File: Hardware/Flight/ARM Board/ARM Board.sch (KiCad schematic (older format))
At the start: 1 part, among them U1 STM32L4x6RxT6

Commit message: Added footprint and sch for SD logger, pull up resistor on data out as per documentation found in Datasheets and Documentation folder
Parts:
- added J?: SD_WM6698CT-ND, symbol ARMlib:SD_WM6698CT-ND
- added R?: R, Resistors_SMD:R_0603, symbol Device:R
- U1: symbol STM32L4x6RxT6 -> symbols:STM32L4x6RxT6
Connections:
- net labels added: VDD
- wire segments 0 -> 3
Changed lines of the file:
@@
-EESchema Schematic File Version 2
-LIBS:power
-LIBS:device
-LIBS:switches
-LIBS:relays
-LIBS:motors
-LIBS:transistors
-LIBS:conn
-LIBS:linear
-LIBS:regul
-LIBS:74xx
-LIBS:cmos4000
-LIBS:adc-dac
-LIBS:memory
-LIBS:xilinx
-LIBS:microcontrollers
-LIBS:dsp
-LIBS:microchip
-LIBS:analog_switches
-LIBS:motorola
-LIBS:texas
-LIBS:intel
-LIBS:audio
-LIBS:interface
-LIBS:digital-audio
-LIBS:philips
-LIBS:display
-LIBS:cypress
-LIBS:siliconi
-LIBS:opto
-LIBS:atmel
-LIBS:contrib
-LIBS:valves
-LIBS:symbols
-EELAYER 25 0
+EESchema Schematic File Version 4
+LIBS:ARM Board-cache
+EELAYER 26 0
 EELAYER END
 $Descr A4 11693 8268
@@
 $EndDescr
 $Comp
-L STM32L4x6RxT6 U1
+L symbols:STM32L4x6RxT6 U1
 U 1 1 5BE24A8B
 P 2300 1950
@@
 $EndComp
 $Comp
-L STM32L4x6RxT6 U1
+L symbols:STM32L4x6RxT6 U1
 U 2 1 5BE24AAA
 P 7050 2200
@@
 	1    0    0    -1
 $EndComp
+$Comp
+L ARMlib:SD_WM6698CT-ND J?
+U 1 1 5BE5108C
+P 8550 5100
+F 0 "J?" H 9028 5202 60  0000 L CNN
+F 1 "SD_WM6698CT-ND" H 9028 5096 60  0000 L CNN
+F 2 "" V 8500 5000 60  0001 C CNN
+F 3 "" V 8500 5000 60  0001 C CNN
+	1    8550 5100
+	1    0    0    -1
+$EndComp
+$Comp
+L Device:R R?
+U 1 1 5BE5134B
+P 7850 4200
+F 0 "R?" H 7920 4246 50  0000 L CNN
+F 1 "R" H 7920 4155 50  0000 L CNN
+F 2 "Resistors_SMD:R_0603" V 7780 4200 50  0001 C CNN
+F 3 "~" H 7850 4200 50  0001 C CNN
+	1    7850 4200
+	1    0    0    -1
+$EndComp
+Wire Wire Line
+	7850 4350 7850 4450
+Wire Wire Line
+	7850 4450 8050 4450
+$Comp
+L power:VDD #PWR?
+U 1 1 5BE51D76
+P 7850 3700
+F 0 "#PWR?" H 7850 3550 50  0001 C CNN
+F 1 "VDD" H 7867 3873 50  0000 C CNN
+F 2 "" H 7850 3700 50  0001 C CNN
+F 3 "" H 7850 3700 50  0001 C CNN
+	1    7850 3700
+	1    0    0    -1
+$EndComp
+Wire Wire Line
+	7850 3700 7850 4050
 $EndSCHEMATC

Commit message: Added footprint and sch for IO connector and USB
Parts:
- added J? (x2): Conn_01x20_Female, ARMlib:IO_Connector, symbol ARMlib:Conn_01x20_Female
- added J?: USB_B_Micro, ARMlib:USB_Micro-B_Amphenol_10118193-0001LF, symbol Connector:USB_B_Micro
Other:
- moved on the sheet: R?, U1A, U1B
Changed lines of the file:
@@
 L symbols:STM32L4x6RxT6 U1
 U 1 1 5BE24A8B
-P 2300 1950
-F 0 "U1" H 3250 2500 60  0000 C CNN
-F 1 "STM32L4x6RxT6" H 3250 2400 60  0000 C CNN
-F 2 "STM32L4x6RxT6:STM32L4x6RxT6" H 3150 2300 60  0001 C CNN
-F 3 "" H 2300 2050 60  0000 C CNN
-	1    2300 1950
+P 5450 2700
+F 0 "U1" H 6400 3250 60  0000 C CNN
+F 1 "STM32L4x6RxT6" H 6400 3150 60  0000 C CNN
+F 2 "STM32L4x6RxT6:STM32L4x6RxT6" H 6300 3050 60  0001 C CNN
+F 3 "" H 5450 2800 60  0000 C CNN
+	1    5450 2700
 	1    0    0    -1
 $EndComp
@@
 L symbols:STM32L4x6RxT6 U1
 U 2 1 5BE24AAA
-P 7050 2200
-F 0 "U1" H 8000 2750 60  0000 C CNN
-F 1 "STM32L4x6RxT6" H 8000 2650 60  0000 C CNN
-F 2 "LQFP64-10x10mm" H 7900 2550 60  0001 C CNN
-F 3 "" H 7050 2300 60  0000 C CNN
-	2    7050 2200
+P 2400 1450
+F 0 "U1" H 3350 2000 60  0000 C CNN
+F 1 "STM32L4x6RxT6" H 3350 1900 60  0000 C CNN
+F 2 "LQFP64-10x10mm" H 3250 1800 60  0001 C CNN
+F 3 "" H 2400 1550 60  0000 C CNN
+	2    2400 1450
 	1    0    0    -1
 $EndComp
@@
 L ARMlib:SD_WM6698CT-ND J?
 U 1 1 5BE5108C
-P 8550 5100
-F 0 "J?" H 9028 5202 60  0000 L CNN
-F 1 "SD_WM6698CT-ND" H 9028 5096 60  0000 L CNN
-F 2 "" V 8500 5000 60  0001 C CNN
-F 3 "" V 8500 5000 60  0001 C CNN
-	1    8550 5100
+P 10300 5050
+F 0 "J?" H 10778 5152 60  0000 L CNN
+F 1 "SD_WM6698CT-ND" H 10778 5046 60  0000 L CNN
+F 2 "" V 10250 4950 60  0001 C CNN
+F 3 "" V 10250 4950 60  0001 C CNN
+	1    10300 5050
 	1    0    0    -1
 $EndComp
@@
 L Device:R R?
 U 1 1 5BE5134B
-P 7850 4200
-F 0 "R?" H 7920 4246 50  0000 L CNN
-F 1 "R" H 7920 4155 50  0000 L CNN
-F 2 "Resistors_SMD:R_0603" V 7780 4200 50  0001 C CNN
-F 3 "~" H 7850 4200 50  0001 C CNN
-	1    7850 4200
+P 9600 4150
+F 0 "R?" H 9670 4196 50  0000 L CNN
+F 1 "R" H 9670 4105 50  0000 L CNN
+F 2 "Resistors_SMD:R_0603" V 9530 4150 50  0001 C CNN
+F 3 "~" H 9600 4150 50  0001 C CNN
+	1    9600 4150
 	1    0    0    -1
 $EndComp
 Wire Wire Line
-	7850 4350 7850 4450
+	9600 4300 9600 4400
 Wire Wire Line
-	7850 4450 8050 4450
+	9600 4400 9800 4400
 $Comp
 L power:VDD #PWR?
 U 1 1 5BE51D76
-P 7850 3700
-F 0 "#PWR?" H 7850 3550 50  0001 C CNN
-F 1 "VDD" H 7867 3873 50  0000 C CNN
-F 2 "" H 7850 3700 50  0001 C CNN
-F 3 "" H 7850 3700 50  0001 C CNN
-	1    7850 3700
+P 9600 3650
+F 0 "#PWR?" H 9600 3500 50  0001 C CNN
+F 1 "VDD" H 9617 3823 50  0000 C CNN
+F 2 "" H 9600 3650 50  0001 C CNN
+F 3 "" H 9600 3650 50  0001 C CNN
+	1    9600 3650
 	1    0    0    -1
 $EndComp
 Wire Wire Line
-	7850 3700 7850 4050
+	9600 3650 9600 4000
+$Comp
+L ARMlib:Conn_01x20_Female J?
+U 1 1 5BE939D5
+P 950 6450
+F 0 "J?" H 944 5175 50  0000 C CNN
+F 1 "Conn_01x20_Female" H 944 5266 50  0000 C CNN
+F 2 "ARMlib:IO_Connector" H 1000 6400 50  0001 C CNN
+F 3 "~" H 1000 6400 50  0001 C CNN
+	1    950  6450
+	-1   0    0    1
+$EndComp
+$Comp
+L ARMlib:Conn_01x20_Female J?
+U 1 1 5BE93A8D
+P 1000 4050
+F 0 "J?" H 994 2775 50  0000 C CNN
+F 1 "Conn_01x20_Female" H 994 2866 50  0000 C CNN
+F 2 "ARMlib:IO_Connector" H 1050 4000 50  0001 C CNN
+F 3 "~" H 1050 4000 50  0001 C CNN
+	1    1000 4050
+	-1   0    0    1
+$EndComp
+$Comp
+L Connector:USB_B_Micro J?
+U 1 1 5BE9421F
+P 1100 1650
+F 0 "J?" H 1155 2117 50  0000 C CNN
+F 1 "USB_B_Micro" H 1155 2026 50  0000 C CNN
+F 2 "ARMlib:USB_Micro-B_Amphenol_10118193-0001LF" H 1250 1600 50  0001 C CNN
+F 3 "~" H 1250 1600 50  0001 C CNN
+	1    1100 1650
+	1    0    0    -1
+$EndComp
 $EndSCHEMATC

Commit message: Added crystal, caps and MsP430
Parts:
- added C1, C2: C_Small, symbol Device:C_Small
- added U2: MSP430FR2355, ARMlib:48-LQFP, symbol MSP430FR2355:MSP430FR2355
- added Y1: Crystal_GND23, ARMlib:MC-306 32.7680K, symbol Device:Crystal_GND23
- gave numbers to parts that had none: 5
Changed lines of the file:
@@
 $EndComp
 $Comp
-L ARMlib:SD_WM6698CT-ND J?
+L ARMlib:SD_WM6698CT-ND J3
 U 1 1 5BE5108C
 P 10300 5050
-F 0 "J?" H 10778 5152 60  0000 L CNN
+F 0 "J3" H 10778 5152 60  0000 L CNN
 F 1 "SD_WM6698CT-ND" H 10778 5046 60  0000 L CNN
 F 2 "" V 10250 4950 60  0001 C CNN
@@
 $EndComp
 $Comp
-L Device:R R?
+L Device:R R1
 U 1 1 5BE5134B
 P 9600 4150
-F 0 "R?" H 9670 4196 50  0000 L CNN
+F 0 "R1" H 9670 4196 50  0000 L CNN
 F 1 "R" H 9670 4105 50  0000 L CNN
 F 2 "Resistors_SMD:R_0603" V 9530 4150 50  0001 C CNN
@@
 	9600 4400 9800 4400
 $Comp
-L power:VDD #PWR?
+L power:VDD #PWR0101
 U 1 1 5BE51D76
 P 9600 3650
-F 0 "#PWR?" H 9600 3500 50  0001 C CNN
+F 0 "#PWR0101" H 9600 3500 50  0001 C CNN
 F 1 "VDD" H 9617 3823 50  0000 C CNN
 F 2 "" H 9600 3650 50  0001 C CNN
@@
 	9600 3650 9600 4000
 $Comp
-L ARMlib:Conn_01x20_Female J?
+L ARMlib:Conn_01x20_Female J4
 U 1 1 5BE939D5
 P 950 6450
-F 0 "J?" H 944 5175 50  0000 C CNN
+F 0 "J4" H 944 5175 50  0000 C CNN
 F 1 "Conn_01x20_Female" H 944 5266 50  0000 C CNN
 F 2 "ARMlib:IO_Connector" H 1000 6400 50  0001 C CNN
@@
 $EndComp
 $Comp
-L ARMlib:Conn_01x20_Female J?
+L ARMlib:Conn_01x20_Female J2
 U 1 1 5BE93A8D
 P 1000 4050
-F 0 "J?" H 994 2775 50  0000 C CNN
+F 0 "J2" H 994 2775 50  0000 C CNN
 F 1 "Conn_01x20_Female" H 994 2866 50  0000 C CNN
 F 2 "ARMlib:IO_Connector" H 1050 4000 50  0001 C CNN
@@
 $EndComp
 $Comp
-L Connector:USB_B_Micro J?
+L Connector:USB_B_Micro J1
 U 1 1 5BE9421F
 P 1100 1650
-F 0 "J?" H 1155 2117 50  0000 C CNN
+F 0 "J1" H 1155 2117 50  0000 C CNN
 F 1 "USB_B_Micro" H 1155 2026 50  0000 C CNN
 F 2 "ARMlib:USB_Micro-B_Amphenol_10118193-0001LF" H 1250 1600 50  0001 C CNN
@@
 	1    0    0    -1
 $EndComp
+$Comp
+L Device:Crystal_GND23 Y1
+U 1 1 5BF7653E
+P 9250 5900
+F 0 "Y1" H 9250 6250 50  0000 L CNN
+F 1 "Crystal_GND23" H 9000 6150 50  0000 L CNN
+F 2 "ARMlib:MC-306 32.7680K" H 9250 5900 50  0001 C CNN
+F 3 "~" H 9250 5900 50  0001 C CNN
+	1    9250 5900
+	1    0    0    -1
+$EndComp
+$Comp
+L Device:C_Small C2
+U 1 1 5BF76C5B
+P 9550 6150
+F 0 "C2" H 9642 6196 50  0000 L CNN
+F 1 "C_Small" H 9642 6105 50  0000 L CNN
+F 2 "" H 9550 6150 50  0001 C CNN
+F 3 "~" H 9550 6150 50  0001 C CNN
+	1    9550 6150
+	1    0    0    -1
+$EndComp
+$Comp
+L Device:C_Small C1
+U 1 1 5BF76CF0
+P 8900 6150
+F 0 "C1" H 8992 6196 50  0000 L CNN
+F 1 "C_Small" H 8992 6105 50  0000 L CNN
+F 2 "" H 8900 6150 50  0001 C CNN
+F 3 "~" H 8900 6150 50  0001 C CNN
+	1    8900 6150
+	1    0    0    -1
+$EndComp
+$Comp
+L MSP430FR2355:MSP430FR2355 U2
+U 1 1 5BF776E6
+P 14350 2100
+F 0 "U2" H 14400 3587 60  0000 C CNN
+F 1 "MSP430FR2355" H 14400 3481 60  0000 C CNN
+F 2 "ARMlib:48-LQFP" H 14350 650 60  0001 C CNN
+F 3 "http://www.ti.com/lit/ds/symlink/msp430fr2355.pdf" H 14350 550 60  0001 C CNN
+F 4 "296-50261-1-ND" H 14350 450 60  0001 C CNN "Digi-Key Part Number"
+	1    14350 2100
+	1    0    0    -1
+$EndComp

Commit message: power supply for stm32
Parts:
- added C? (x3): 100nF, symbol Device:C
- added C?: 1uF, symbol Device:C
- added C?: 10uF, symbol Device:C
- added C?: 100uF, symbol Device:C
- added L?: Ferrite_Bead, symbol Device:Ferrite_Bead
- J2, J4: symbol ARMlib:Conn_01x20_Female -> ARM-Board-rescue:Conn_01x20_Female-ARMlib
- J3: symbol ARMlib:SD_WM6698CT-ND -> ARM-Board-rescue:SD_WM6698CT-ND-ARMlib
- U1: symbol symbols:STM32L4x6RxT6 -> ARM-Board-rescue:STM32L4x6RxT6-symbols
- U2: symbol MSP430FR2355:MSP430FR2355 -> ARM-Board-rescue:MSP430FR2355-MSP430FR2355
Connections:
- net labels added: GND
- wire segments 3 -> 35
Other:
- note added: "TODO\n-ADD RAM\n-ADD CANBUS\n-ADD USB TO UART\n-POWER SWITCH"

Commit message: Added USB to UART and connected XTAL
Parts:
- added C? (x2): 47pF, symbol Device:C
- added C? (x2): 100nF, symbol Device:C
- added C?: 4.7uF, symbol Device:C
- added FB?: Ferrite_Bead, symbol Device:Ferrite_Bead
- added J?: SD_WM6698CT-ND, symbol ARM-Board-rescue:SD_WM6698CT-ND-ARMlib
- added J?: USB_OTG, symbol Connector:USB_OTG
- added R?: R, Resistors_SMD:R_0603, symbol Device:R
- added R? (x2): 27, symbol Device:R
- added R? (x4): 10K, symbol Device:R
- added U?: FT230XS, Package_SO:SSOP-16_3.9x4.9mm_P0.635mm, symbol Interface_USB:FT230XS
- U1: Package (none) -> 64LQFP
- U1: footprint LQFP64-10x10mm -> STM32L4x6RxT6:STM32L4x6RxT6
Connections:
- net labels added: RXD, TXD, VBUS, VCCIO, ~CTS, ~RTS
- wire segments 35 -> 114
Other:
- moved on the sheet: C1, C2, J3, R1, U1A, U2, Y1

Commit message: Completion of previous commit
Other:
- note added: "Ground other XTAL pins? Floating in datasheet...\n"
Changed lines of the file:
@@
 Wire Wire Line
 	6000 7250 6000 7400
+Text Notes 4000 7400 0    50   ~ 0
+Ground other XTAL pins? Floating in datasheet...\n
 $EndSCHEMATC

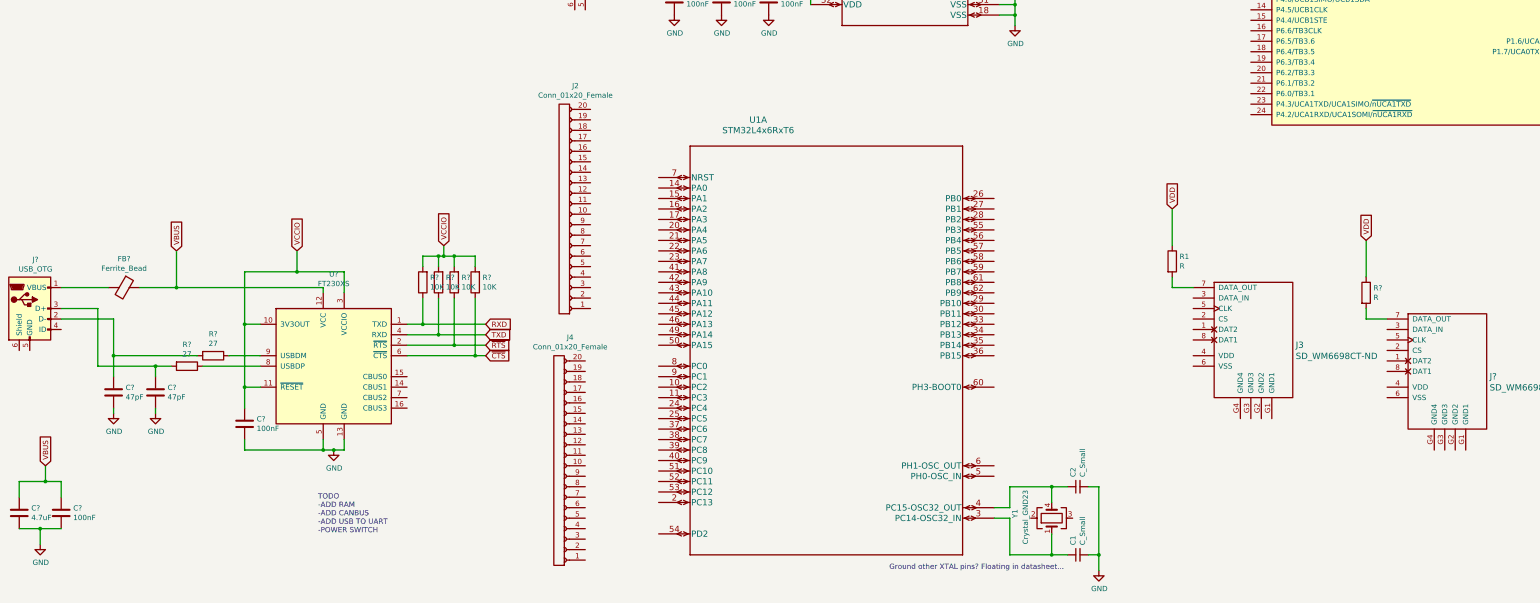
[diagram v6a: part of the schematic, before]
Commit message: RAM and cleanup
Added RAM module, seperate sch for USB to UART, SPI pin net flags
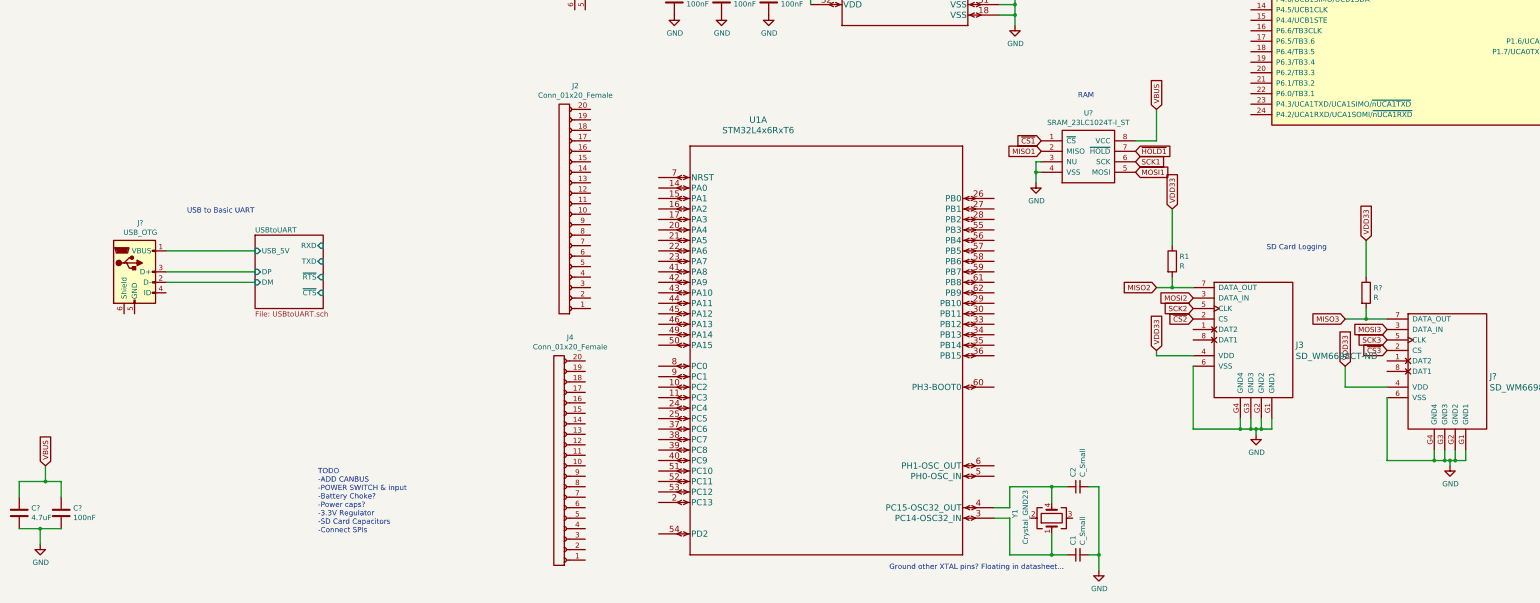
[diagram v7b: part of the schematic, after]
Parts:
- removed C? (x2): 47pF, symbol Device:C
- removed C?: 100nF, symbol Device:C
- removed FB?: Ferrite_Bead, symbol Device:Ferrite_Bead
- removed R? (x2): 27, symbol Device:R
- removed R? (x4): 10K, symbol Device:R
- removed U?: FT230XS, Package_SO:SSOP-16_3.9x4.9mm_P0.635mm, symbol Interface_USB:FT230XS
- added U?: SRAM_23LC1024T-I_ST, Housings_SSOP:TSSOP-8_4.4x3mm_Pitch0.65mm, symbol ARMlib:SRAM_23LC1024T-I_ST
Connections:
- net GND: now also J3.6 (VSS), J3.G1 (GND1), J3.G2 (GND2), J3.G3 (GND3), J3.G4 (GND4), J?.6 (VSS), J?.G1 (GND1), J?.G2 (GND2), J?.G3 (GND3), J?.G4 (GND4), U?.3 (NU), U?.4 (VSS)
- net VBUS: now also U?.8 (VCC)
- net VDD: no longer R1.1, R?.1
- net ~CS2: now reaches J3.2 (CS)
- net MOSI2: now reaches J3.3 (DATA_IN)
- net VDD33: now reaches J3.4 (VDD)
- net VDD33: now also J?.4 (VDD), R1.1, R?.1
- net SCK2: now reaches J3.5 (CLK)
- net MISO2: now reaches J3.7 (DATA_OUT), R1.2
- net ~CS3: now reaches J?.2 (CS)
- net MOSI3: now reaches J?.3 (DATA_IN)
- net SCK3: now reaches J?.5 (CLK)
- net MISO3: now reaches J?.7 (DATA_OUT), R?.2
- net USBtoUART/DP: now reaches J?.3 (D+)
- net USBtoUART/DM: now reaches J?.2 (D-)
- net USBtoUART/USB_5V: now reaches J?.1 (VBUS)
- new net MISO1: U?.2 (MISO)
- new net MOSI1: U?.5 (MOSI)
- new net SCK1: U?.6 (SCK)
- new net ~CS1: U?.1 (~CS)
- new net ~HOLD1: U?.7 (~HOLD)
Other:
- note added: "RAM"
- note added: "SD Card Logging"
- note added: "TODO\n-ADD CANBUS\n-POWER SWITCH & input\n-Battery Choke?\n-Power caps?\n-3.3V Regulator\n-SD Card Capacitors\n-Connect SPIs"
- note added: "USB to Basic UART"
- note removed: "TODO\n-ADD RAM\n-ADD CANBUS\n-ADD USB TO UART\n-POWER SWITCH"
- moved on the sheet: J?
